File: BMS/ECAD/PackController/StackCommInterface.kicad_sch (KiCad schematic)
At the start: 31 parts, among them T1 HM2116ANL, T2 HM2116ANL

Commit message: close to finish BMS master, only some footprints needed
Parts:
- added R310: 10kR, Resistor_SMD:R_0603_1608Metric, symbol Device:R
- U301: renamed from U1; value (none) -> TLE9015; footprint (none) -> Package_QFP:TQFP-48-1EP_7x7mm_P0.5mm_EP5x5mm
- renumbered C16 to C301, C15 to C302, C14 to C303, C13 to C304, C64 to C305, C6 to C306, C8 to C307, C66 to C308, C65 to C309, C7 to C310, C9 to C311, C67 to C312, C10 to C313, C12 to C314, C17 to C315, C11 to C316, R25 to R301, R18 to R302, R28 to R303, R21 to R304, R20 to R305, R27 to R306, R26 to R307, R19 to R308, R29 to R309, R24 to R311, R22 to R312, R23 to R313, T1 to T301, T2 to T302
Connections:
- net ERRQ: now also R310.1
- net VDDC: now also R310.2
- net at C302.1, U301.31 (VregOut_VDDA): no longer C303.1, U301.30 (VIO)
- new net +3.3V: C303.1, U301.30 (VIO)

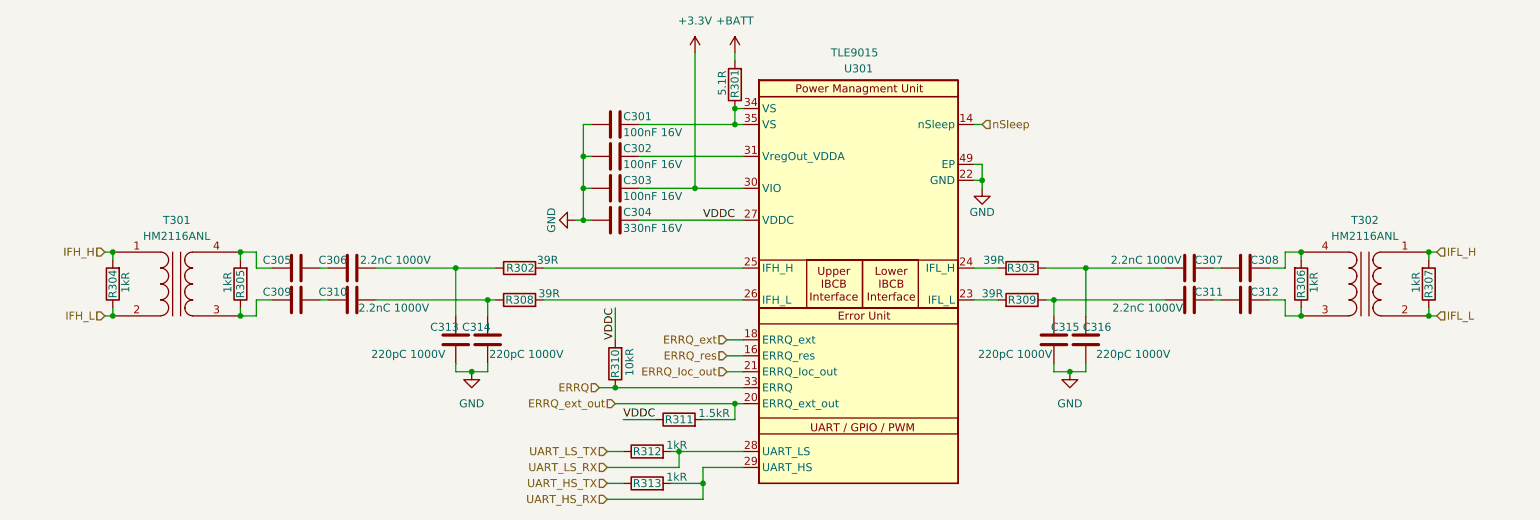
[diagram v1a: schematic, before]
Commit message: finalised schematic of pack controller
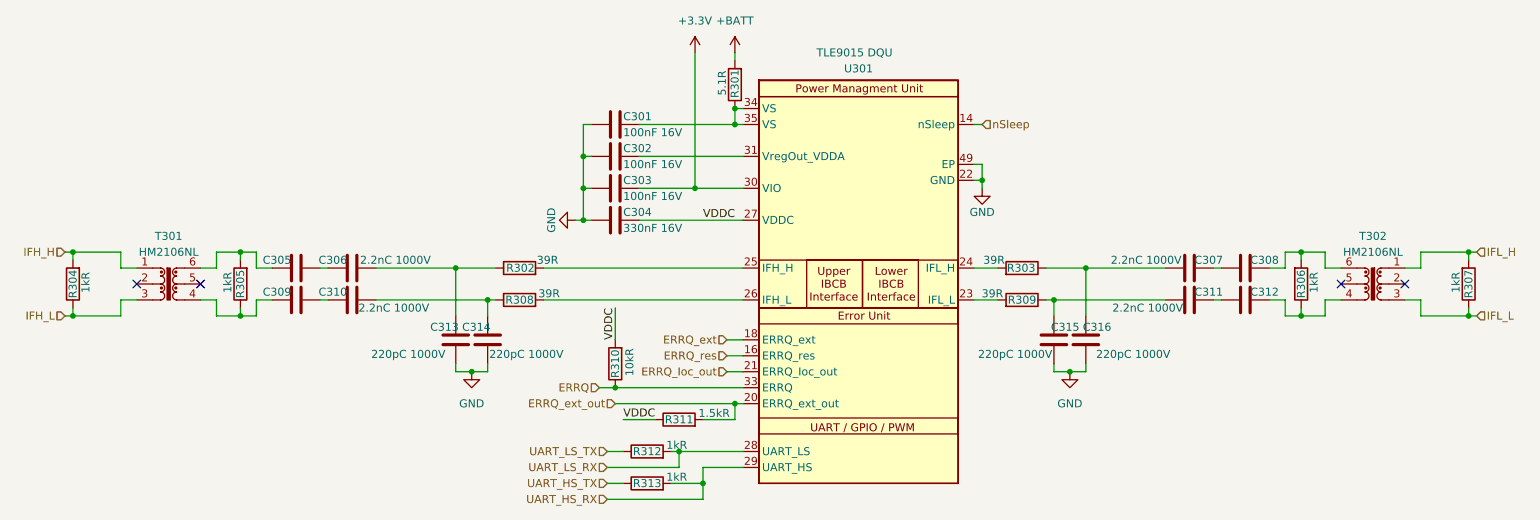
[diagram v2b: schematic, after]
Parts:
- T301, T302: value HM2116ANL -> HM2106NL; footprint (none) -> EKartParts:Pulse_HM2106NL; symbol Device:Transformer_1P_1S -> Transformer:Wuerth_750315371
- U301: value TLE9015 -> TLE9015 DQU
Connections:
- net IFH_L: now also T301.3; no longer T301.2 (AB)
- net IFL_L: now also T302.3; no longer T302.2 (AB)
- net at C309.2, R305.1: now also T301.4; no longer T301.3 (SA)
- net at C305.2, R305.2: now also T301.6; no longer T301.4 (SB)
- net at C312.2, R306.1: now also T302.4; no longer T302.3 (SA)
- net at C308.2, R306.2: now also T302.6; no longer T302.4 (SB)
- no-connect marks 0 -> 4
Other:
- moved on the sheet: R304, R307

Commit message: yes
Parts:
- C304: value 330nF 16V -> 330nF 50V; footprint Capacitor_SMD:C_1206_3216Metric -> Capacitor_SMD:C_0805_2012Metric
- C305, C306, C307, C308, C310, C311, C312: value 2.2nC 1000V -> 2.2nC 100V; footprint Capacitor_SMD:C_1206_3216Metric -> Capacitor_SMD:C_0603_1608Metric
- C309: footprint Capacitor_SMD:C_1206_3216Metric -> Capacitor_SMD:C_0603_1608Metric
- C313, C314, C315, C316: value 220pC 1000V -> 220pC 100V; footprint Capacitor_SMD:C_1206_3216Metric -> Capacitor_SMD:C_0603_1608Metric
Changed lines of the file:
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@@
 			)
 		)
-		(property "Value" "330nF 16V"
+		(property "Value" "330nF 50V"
 			(at 121.92 78.74 90)
 			(show_name no)
@@
 			)
 		)
-		(property "Footprint" "Capacitor_SMD:C_1206_3216Metric"
+		(property "Footprint" "Capacitor_SMD:C_0805_2012Metric"
 			(at 116.84 78.4352 0)
 			(hide yes)
@@
 			)
 		)
-		(property "Value" "220pC 1000V"
+		(property "Value" "220pC 100V"
 			(at 190.246 98.806 0)
 			(show_name no)
@@
 			)
 		)
-		(property "Footprint" "Capacitor_SMD:C_1206_3216Metric"
+		(property "Footprint" "Capacitor_SMD:C_0603_1608Metric"
 			(at 189.5348 100.33 0)
 			(hide yes)
@@
 			)
 		)
-		(property "Footprint" "Capacitor_SMD:C_1206_3216Metric"
+		(property "Footprint" "Capacitor_SMD:C_0603_1608Metric"
 			(at 66.04 91.1352 0)
 			(hide yes)
@@
 			)
 		)
-		(property "Value" "2.2nC 1000V"
+		(property "Value" "2.2nC 100V"
 			(at 70.866 81.28 90)
 			(hide yes)
@@
 			)
 		)
-		(property "Footprint" "Capacitor_SMD:C_1206_3216Metric"
+		(property "Footprint" "Capacitor_SMD:C_0603_1608Metric"
 			(at 66.04 86.0552 0)
 			(hide yes)
@@
 			)
 		)
-		(property "Value" "2.2nC 1000V"
+		(property "Value" "2.2nC 100V"
 			(at 80.01 83.82 90)
 			(show_name no)
@@
 			)
 		)
-		(property "Footprint" "Capacitor_SMD:C_1206_3216Metric"
+		(property "Footprint" "Capacitor_SMD:C_0603_1608Metric"
 			(at 74.93 86.0552 0)
 			(hide yes)
@@
 			)
 		)
-		(property "Value" "2.2nC 1000V"
+		(property "Value" "2.2nC 100V"
 			(at 211.074 91.44 90)
 			(show_name no)
@@
 			)
 		)
-		(property "Footprint" "Capacitor_SMD:C_1206_3216Metric"
+		(property "Footprint" "Capacitor_SMD:C_0603_1608Metric"
 			(at 215.9 91.1352 0)
 			(hide yes)
@@
 			)
 		)
-		(property "Value" "2.2nC 1000V"
+		(property "Value" "2.2nC 100V"
 			(at 219.964 81.28 90)
 			(hide yes)
@@
 			)
 		)
-		(property "Footprint" "Capacitor_SMD:C_1206_3216Metric"
+		(property "Footprint" "Capacitor_SMD:C_0603_1608Metric"
 			(at 224.79 86.0552 0)
 			(hide yes)
@@
 			)
 		)
-		(property "Value" "220pC 1000V"
+		(property "Value" "220pC 100V"
 			(at 81.788 98.806 0)
 			(show_name no)
@@
 			)
 		)
-		(property "Footprint" "Capacitor_SMD:C_1206_3216Metric"
+		(property "Footprint" "Capacitor_SMD:C_0603_1608Metric"
 			(at 96.2152 100.33 0)
 			(hide yes)
@@
 			)
 		)
-		(property "Value" "220pC 1000V"
+		(property "Value" "220pC 100V"
 			(at 209.042 98.806 0)
 			(show_name no)
@@
 			)
 		)
-		(property "Footprint" "Capacitor_SMD:C_1206_3216Metric"
+		(property "Footprint" "Capacitor_SMD:C_0603_1608Metric"
 			(at 194.6148 100.33 0)
 			(hide yes)
@@
 			)
 		)
-		(property "Value" "2.2nC 1000V"
+		(property "Value" "2.2nC 100V"
 			(at 79.756 91.44 90)
 			(show_name no)
@@
 			)
 		)
-		(property "Footprint" "Capacitor_SMD:C_1206_3216Metric"
+		(property "Footprint" "Capacitor_SMD:C_0603_1608Metric"
 			(at 74.93 91.1352 0)
 			(hide yes)
@@
 			)
 		)
-		(property "Value" "2.2nC 1000V"
+		(property "Value" "2.2nC 100V"
 			(at 210.82 83.82 90)
 			(show_name no)
@@
 			)
 		)
-		(property "Footprint" "Capacitor_SMD:C_1206_3216Metric"
+		(property "Footprint" "Capacitor_SMD:C_0603_1608Metric"
 			(at 215.9 86.0552 0)
 			(hide yes)
@@
 			)
 		)
-		(property "Value" "2.2nC 1000V"
+		(property "Value" "2.2nC 100V"
 			(at 219.964 91.44 90)
 			(hide yes)
@@
 			)
 		)
-		(property "Footprint" "Capacitor_SMD:C_1206_3216Metric"
+		(property "Footprint" "Capacitor_SMD:C_0603_1608Metric"
 			(at 224.79 91.1352 0)
 			(hide yes)
@@
 			)
 		)
-		(property "Value" "220pC 1000V"
+		(property "Value" "220pC 100V"
 			(at 100.584 98.806 0)
 			(show_name no)
@@
 			)
 		)
-		(property "Footprint" "Capacitor_SMD:C_1206_3216Metric"
+		(property "Footprint" "Capacitor_SMD:C_0603_1608Metric"
 			(at 101.2952 100.33 0)
 			(hide yes)
